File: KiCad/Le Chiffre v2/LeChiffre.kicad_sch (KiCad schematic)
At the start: 133 parts, among them J1 Conn_01x06_Socket, J2 Conn_01x04_Female, SW1 SW_Push, SW10 SW_Push, SW11 SW_Push, SW12 SW_Push, SW13 SW_Push, SW14 SW_Push, SW15 SW_Push, SW16 SW_Push, SW17 SW_Push, SW18 SW_Push, SW19 SW_Push, SW2 SW_Push, SW20 SW_Push, SW21 SW_Push, SW22 SW_Push, SW23 SW_Push, SW24 SW_Push, SW25 SW_Push, SW26 SW_Push, SW27 SW_Push, SW28 SW_Push, SW29 SW_Push, SW3 SW_Push, SW30 SW_Push, SW31 SW_Push, SW32 SW_Push, SW33 SW_Push, SW34 SW_Push, SW35 SW_Push, SW36 Rotary_Encoder_Switch, SW37 SW_Push, SW38 SW_Push, SW39 SW_Push, SW4 SW_Push, SW5 SW_Push, SW6 SW_Push, SW7 SW_Push, SW8 SW_Push, SW9 SW_Push, U1 pro-micro-controller, U2 SN74HC595

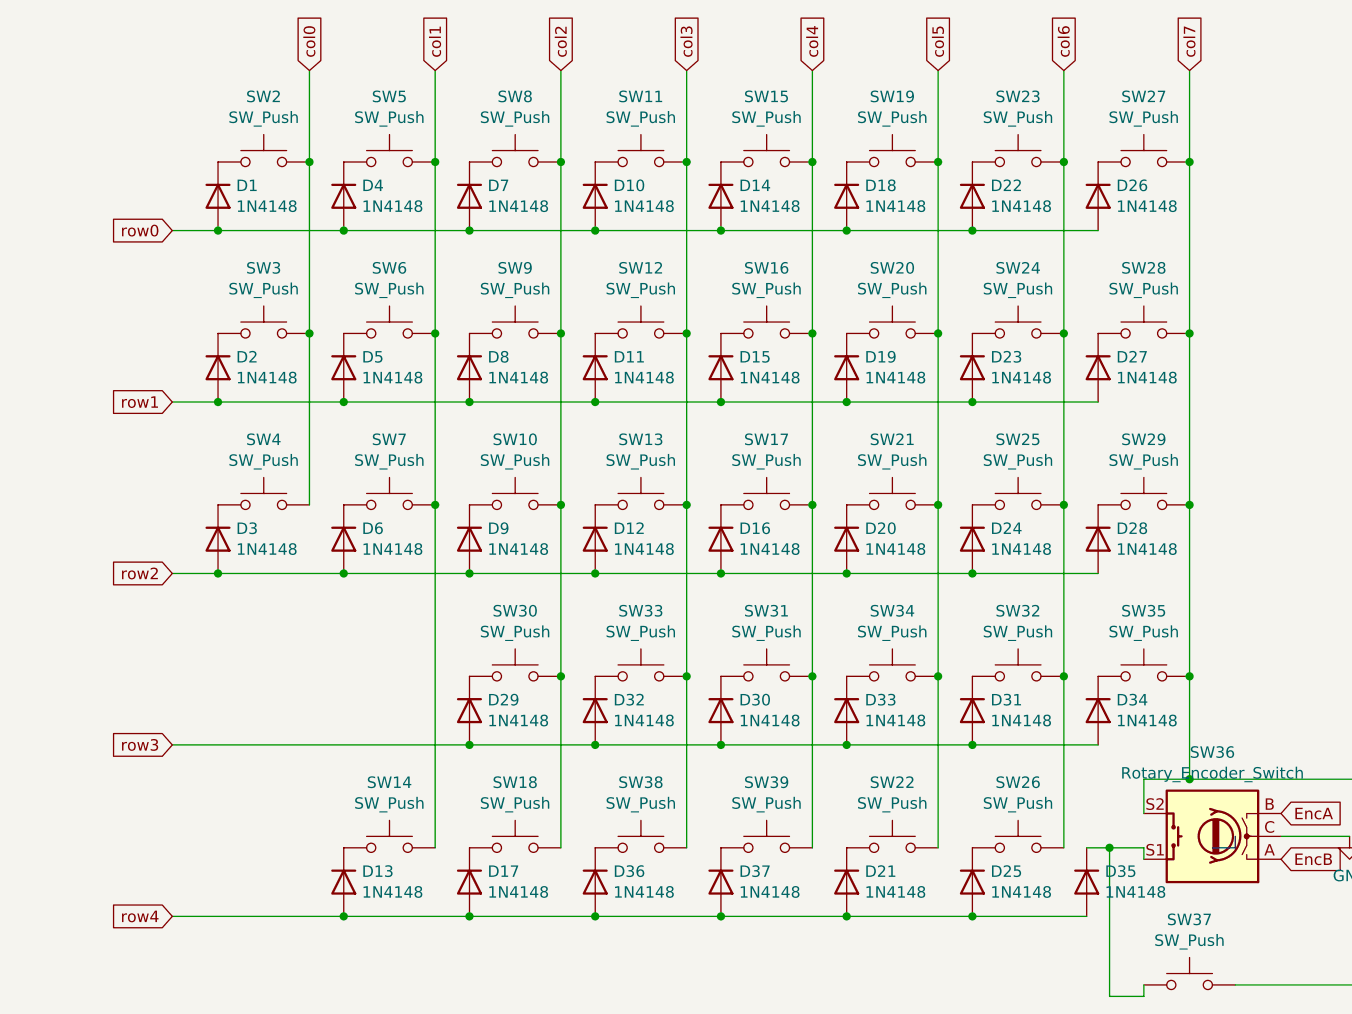
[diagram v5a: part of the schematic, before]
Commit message: fixed diode orientation to work with shift register
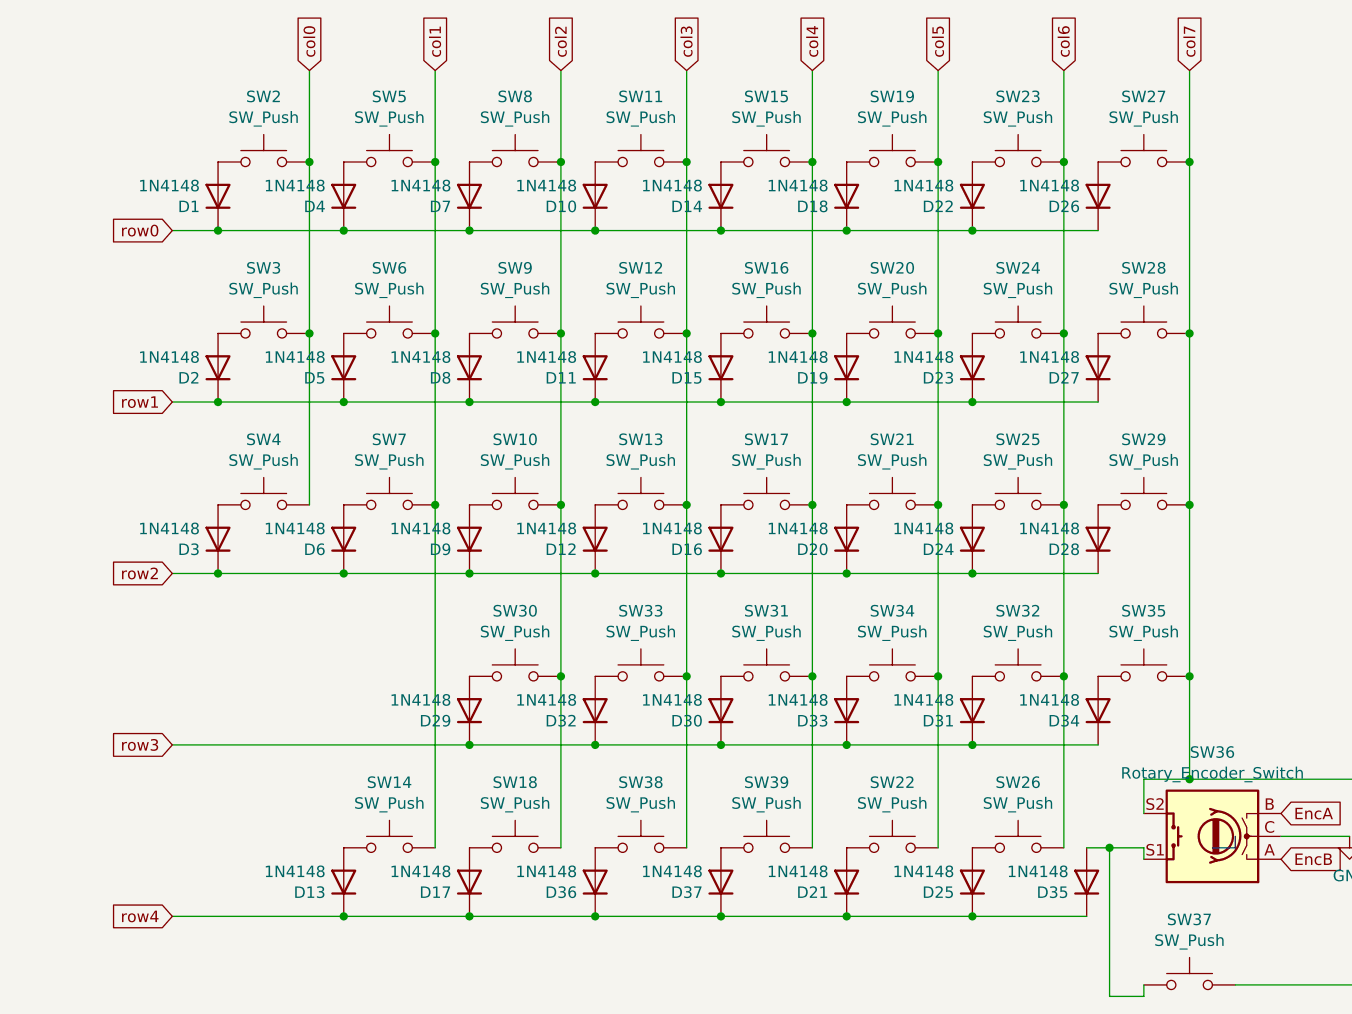
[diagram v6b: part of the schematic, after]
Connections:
- net row0: now also D1.1 (K), D10.1 (K), D14.1 (K), D18.1 (K), D22.1 (K), D26.1 (K), D4.1 (K), D7.1 (K); no longer D1.2 (A), D10.2 (A), D14.2 (A), D18.2 (A), D22.2 (A), D26.2 (A), D4.2 (A), D7.2 (A)
- net row1: now also D11.1 (K), D15.1 (K), D19.1 (K), D2.1 (K), D23.1 (K), D27.1 (K), D5.1 (K), D8.1 (K); no longer D11.2 (A), D15.2 (A), D19.2 (A), D2.2 (A), D23.2 (A), D27.2 (A), D5.2 (A), D8.2 (A)
- net row2: now also D12.1 (K), D16.1 (K), D20.1 (K), D24.1 (K), D28.1 (K), D3.1 (K), D6.1 (K), D9.1 (K); no longer D12.2 (A), D16.2 (A), D20.2 (A), D24.2 (A), D28.2 (A), D3.2 (A), D6.2 (A), D9.2 (A)
- net row3: now also D29.1 (K), D30.1 (K), D31.1 (K), D32.1 (K), D33.1 (K), D34.1 (K); no longer D29.2 (A), D30.2 (A), D31.2 (A), D32.2 (A), D33.2 (A), D34.2 (A)
- net row4: now also D13.1 (K), D17.1 (K), D21.1 (K), D25.1 (K), D35.1 (K), D36.1 (K), D37.1 (K); no longer D13.2 (A), D17.2 (A), D21.2 (A), D25.2 (A), D35.2 (A), D36.2 (A), D37.2 (A)
- net at SW28.1: now also D27.2 (A); no longer D27.1 (K)
- net at SW22.1: now also D21.2 (A); no longer D21.1 (K)
- net at SW18.1: now also D17.2 (A); no longer D17.1 (K)
- net at SW34.1: now also D33.2 (A); no longer D33.1 (K)
- net at SW31.1: now also D30.2 (A); no longer D30.1 (K)
- net at SW12.1: now also D11.2 (A); no longer D11.1 (K)
- net at SW16.1: now also D15.2 (A); no longer D15.1 (K)
- net at SW3.1: now also D2.2 (A); no longer D2.1 (K)
- net at SW9.1: now also D8.2 (A); no longer D8.1 (K)
- net at SW6.1: now also D5.2 (A); no longer D5.1 (K)
- net at SW20.1: now also D19.2 (A); no longer D19.1 (K)
- net at SW24.1: now also D23.2 (A); no longer D23.1 (K)
- net at SW19.1: now also D18.2 (A); no longer D18.1 (K)
- net at SW8.1: now also D7.2 (A); no longer D7.1 (K)
- net at SW27.1: now also D26.2 (A); no longer D26.1 (K)
- net at SW15.1: now also D14.2 (A); no longer D14.1 (K)
- net at SW33.1: now also D32.2 (A); no longer D32.1 (K)
- net at SW11.1: now also D10.2 (A); no longer D10.1 (K)
- net at SW2.1: now also D1.2 (A); no longer D1.1 (K)
- net at SW5.1: now also D4.2 (A); no longer D4.1 (K)
- net at SW23.1: now also D22.2 (A); no longer D22.1 (K)
- net at SW30.1: now also D29.2 (A); no longer D29.1 (K)
- net at SW21.1: now also D20.2 (A); no longer D20.1 (K)
- net at SW35.1: now also D34.2 (A); no longer D34.1 (K)
- net at SW7.1: now also D6.2 (A); no longer D6.1 (K)
- net at SW17.1: now also D16.2 (A); no longer D16.1 (K)
- net at SW10.1: now also D9.2 (A); no longer D9.1 (K)
- net at SW32.1: now also D31.2 (A); no longer D31.1 (K)
- net at SW4.1: now also D3.2 (A); no longer D3.1 (K)
- net at SW25.1: now also D24.2 (A); no longer D24.1 (K)
- net at SW13.1: now also D12.2 (A); no longer D12.1 (K)
- net at SW29.1: now also D28.2 (A); no longer D28.1 (K)
- net at SW14.1: now also D13.2 (A); no longer D13.1 (K)
- net at SW26.1: now also D25.2 (A); no longer D25.1 (K)
- net at SW36.S1, SW37.1: now also D35.2 (A); no longer D35.1 (K)
- net at SW39.1: now also D37.2 (A); no longer D37.1 (K)
- net at SW38.1: now also D36.2 (A); no longer D36.1 (K)
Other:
- moved on the sheet: D1, D10, D11, D12, D13, D14, D15, D16, D17, D18, D19, D2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
